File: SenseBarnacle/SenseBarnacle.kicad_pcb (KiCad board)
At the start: 4 copper layers, 82.6 x 35.5 mm, 104 parts, among them J1 USB_B_Mini, J2 Debug, J3 Power, J5 I2C_OLED_Display, J6 Conn_02x35_JumperluxCardEdge, J7 Conn_02x35_JumperluxCardEdge, SW1 USB BOOT, U1 LM324, U13 CH446X, U14 CH446X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

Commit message: add ADC resistors
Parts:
- added R39: 2.2K, Resistor_SMD:R_0805_2012Metric_Pad1.20x1.40mm_HandSolder, F.Cu at (94.0, 144.1)
- added R40: 2.2K, Resistor_SMD:R_0805_2012Metric_Pad1.20x1.40mm_HandSolder, F.Cu at (92.1, 144.1)
- added R41: 2.2K, Resistor_SMD:R_0805_2012Metric_Pad1.20x1.40mm_HandSolder, F.Cu at (90.2, 144.1)
- added R42: 2.2K, Resistor_SMD:R_0805_2012Metric_Pad1.20x1.40mm_HandSolder, F.Cu at (88.3, 144.1)
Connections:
- JP4 pad 3: ADC_1_RP -> unconnected-(JP4-B-Pad3)
- U2 pad 1: Net-(JP5-C) -> Net-(U2A--)
- U2 pad 13: Net-(JP2-C) -> Net-(U2D--)
- U2 pad 14: Net-(JP2-C) -> Net-(U2D--)
- U2 pad 2: Net-(JP5-C) -> Net-(U2A--)
- U2 pad 6: Net-(JP4-C) -> Net-(U2B--)
- U2 pad 7: Net-(JP4-C) -> Net-(U2B--)
- U2 pad 8: Net-(JP3-C) -> Net-(U2C--)
- U2 pad 9: Net-(JP3-C) -> Net-(U2C--)

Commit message: Finished routing
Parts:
- removed the U12 at (50.2, 142.9)
- added U5: ~, JumperlessFootprints:QA503C, F.Cu at (50.1, 142.9)
- moved SW1 1.17 mm to (116.1, 145.0)
- moved TP16 0.31 mm to (121.4, 168.6)
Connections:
- JP4 pad 3: unconnected-(JP4-B-Pad3) -> ADC_1_RP
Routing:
- net LED_GND: track 7.62 -> 422.1 mm, vias 0 -> 21
- net +3V3: track 7.62 -> 226.6 mm, vias 0 -> 13
- net LED_5V: track 0.00 -> 179.3 mm, vias 0 -> 4
- net -3.5V: track 0.00 -> 132.8 mm, vias 0 -> 2
- net LED_DATA_IN: track 0.00 -> 116.9 mm, vias 0 -> 4
- net BOTTOM_RAIL_POS: track 0.00 -> 112.0 mm, vias 0 -> 4
- net TOP_RAIL_NEG: track 0.00 -> 105.6 mm, vias 0 -> 5
- net TOP_RAIL_POS: track 0.00 -> 104.5 mm, vias 0 -> 4
- net BOTTOM_RAIL_NEG: track 0.00 -> 100.3 mm, vias 0 -> 3
- net I2C_SCL: track 0.00 -> 93.0 mm, vias 0 -> 4
- net I2C_SDA: track 0.00 -> 91.1 mm, vias 0 -> 4
- net SW_PUSH: track 3.95 -> 94.5 mm, vias 0 -> 4
- net SW_C: track 5.74 -> 92.2 mm, vias 0 -> 4
- net +18V: track 0.00 -> 83.4 mm, vias 0 -> 4
- net SW_D: track 4.91 -> 87.4 mm, vias 0 -> 4
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
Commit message: Update SenseBarnacle.kicad_pcb
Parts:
- moved C6 109.6 mm to (117.2, 56.2)
- moved R13 109.6 mm to (86.9, 39.9)
- moved R15 109.6 mm to (89.0, 39.9)
- moved R17 109.6 mm to (91.0, 39.9)
- moved R5 109.6 mm to (40.0, 55.2)
- moved C1 109.6 mm to (117.4, 42.8)
- moved C12 109.6 mm to (102.7, 47.4)
- moved C14 109.6 mm to (78.1, 40.8)
- moved C15 109.6 mm to (79.2, 42.8)
- moved C18 109.6 mm to (54.2, 59.8)
- moved C23 109.6 mm to (54.2, 57.9)
- moved J3 109.6 mm to (41.5, 30.8)
- moved J5 109.6 mm to (61.2, 34.6)
- moved J7 109.6 mm to (78.3, 63.9)
- moved JP2 109.6 mm to (94.3, 45.9)
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
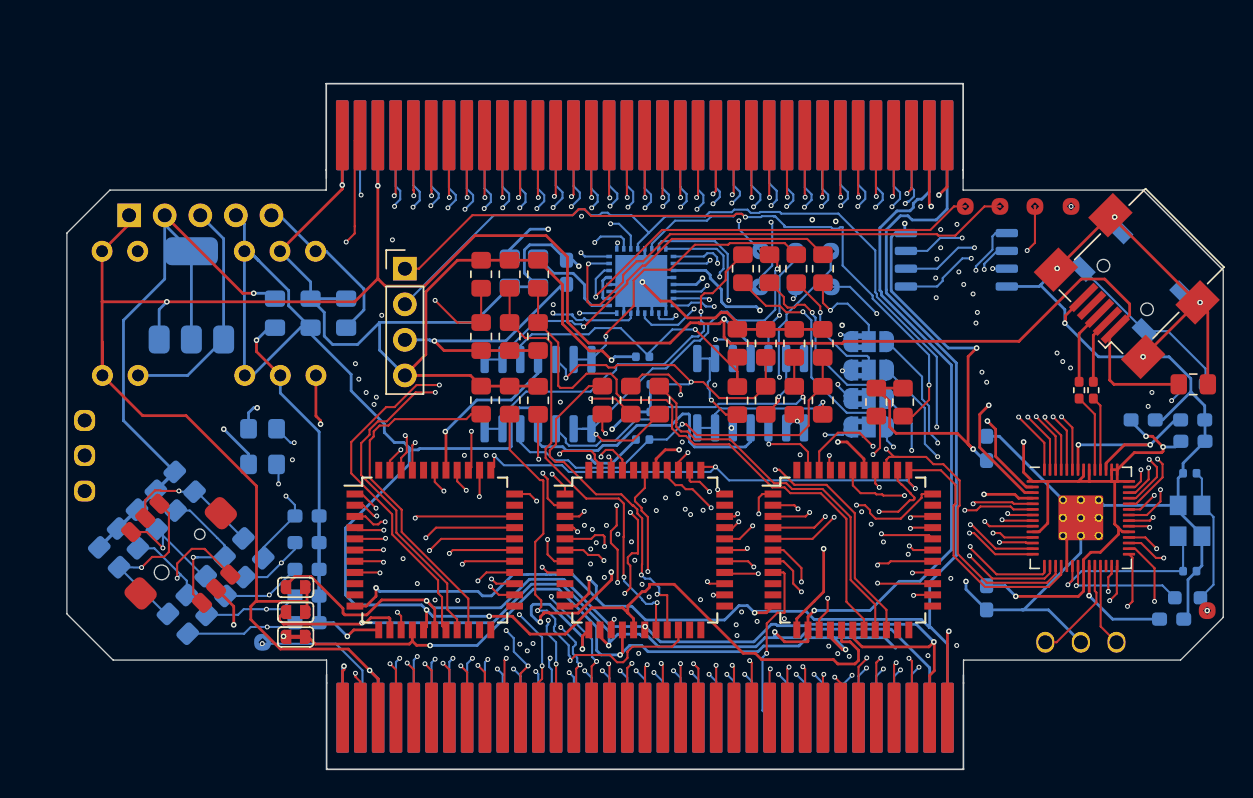
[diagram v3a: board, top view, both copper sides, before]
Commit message: Added silkscreen
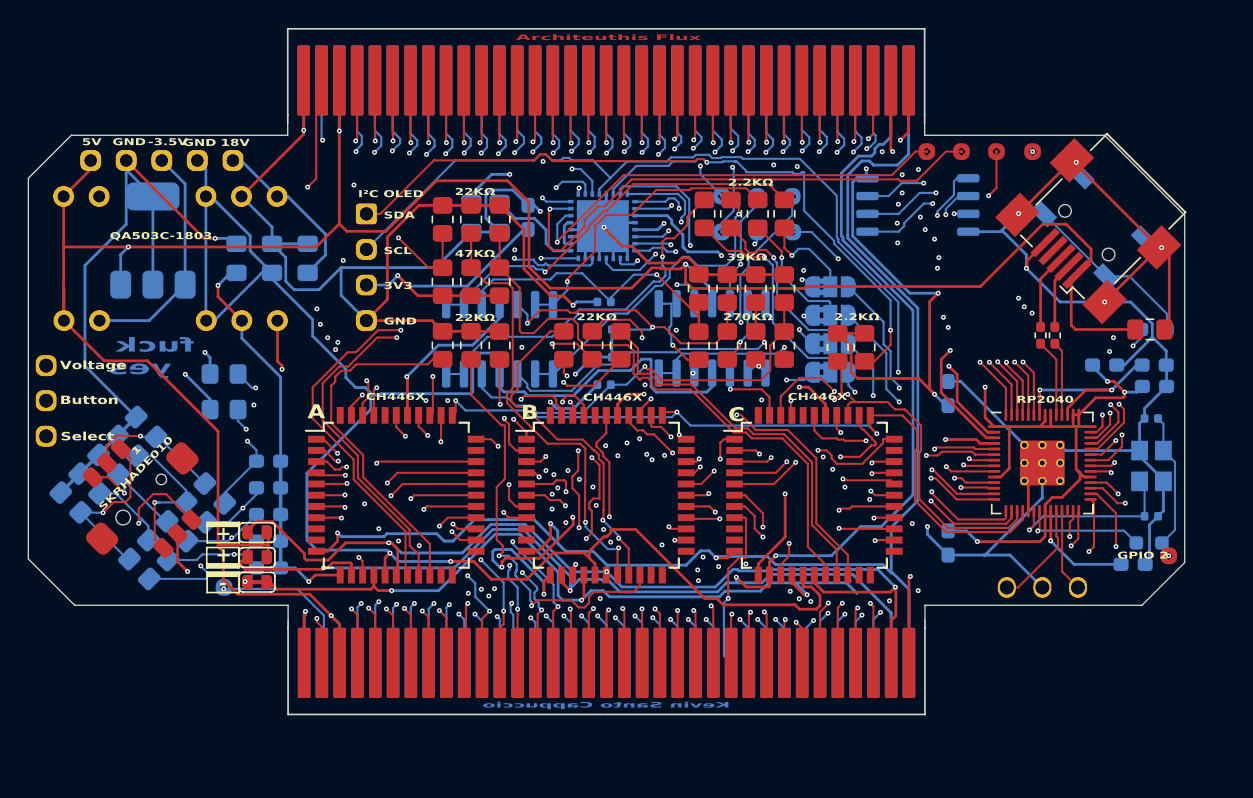
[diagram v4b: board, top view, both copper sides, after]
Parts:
- U12, U5: value ~ -> QA503C
- U4: value ~ -> SKRHAD010
- moved C1 4.99 mm to (114.4, 38.9)
- moved TP10 4.81 mm to (83.8, 29.4)
- moved C3 4.78 mm to (114.7, 41.4)
- moved U15 4.78 mm to (90.8, 50.3)
- moved J6 4.78 mm to (75.5, 23.7)
- moved U6 4.78 mm to (75.3, 31.5)
- moved U8 4.78 mm to (97.8, 30.0)
- moved R30 4.78 mm to (47.6, 50.6)
- moved R32 4.78 mm to (44.9, 53.3)
- moved R33 4.78 mm to (38.6, 49.9)
- moved R6 4.78 mm to (42.2, 56.0)
- moved U13 4.78 mm to (61.0, 50.3)
- moved JP2 4.78 mm to (91.5, 42.0)
- moved JP3 4.78 mm to (91.5, 39.9)
- moved JP4 4.78 mm to (91.5, 37.9)
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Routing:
- net SW_A: track 86.7 -> 89.4 mm
- net LED_DATA_IN: track 116.9 -> 118.8 mm
- net +3V3: track 226.6 -> 227.5 mm
- net Net-(U14-Y2): track 25.4 -> 24.5 mm
- net +18V: track 83.4 -> 84.0 mm
- net Select_Probe: track 15.5 -> 16.1 mm
- net Net-(U13-Y1): track 37.0 -> 37.6 mm
- net 33: track 66.3 -> 65.8 mm
- net TOP_RAIL_POS: track 104.5 -> 105.0 mm
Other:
- board text added: "+"
- board text added: "-"
- board text added: "-3.5V"
- board text added: "0"
- board text added: "0Ω"
- board text added: "1"
- board text added: "18V"
- board text added: "2"
- board text added: "2.2KΩ"
- board text added: "22KΩ"
- board text added: "270KΩ"
- board text added: "3"
- board text added: "39KΩ"
- board text added: "3V3"
- board text added: "47KΩ"
- board text added: "5V"
- board text added: "A"
- board text added: "AK4619"
- board text added: "AK4619 ADC"
- board text added: "Architeuthis Flux"
- board text added: "B"
- board text added: "BOOT"
- board text added: "Button"
- board text added: "C"
- board text added: "CH446X"
- board text added: "GND"
- board text added: "GPIO 2"
- board text added: "I²C OLED"
- board text added: "Kevin Santo Cappuccio"
- board text added: "LED Data"
- board text added: "QA503C-1803"
- board text added: "RP2040"
- board text added: "RP2040 ADC"
- board text added: "SCL"
- board text added: "SDA"
- board text added: "SKRHADE010"
- board text added: "Select"
- board text added: "Sense Barnacle"
- board text added: "Voltage"
- board text added: "Y0"
- board text added: "Y3"
- board text added: "fuck yes"
